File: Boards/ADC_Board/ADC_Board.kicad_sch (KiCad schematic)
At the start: 52 parts, among them J1 DE9_Pins, J10 Conn_01x04, J11 Conn_01x03, J12 Conn_01x03, J13 Conn_01x03, J14 Conn_01x03, J15 Conn_01x03, J17 Conn_01x04, J18 Conn_01x04, J19 Conn_01x04, J2 USB_B_Micro, J20 Conn_01x04, J21 Conn_01x04, J3 Conn_02x05_Odd_Even, J4 Conn_01x05, J5 Conn_01x05, J6 Conn_01x05, J7 Conn_01x03, J8 Conn_01x03, J9 DE9_Socket, U1 STM32G0B1RCTx, U5 BD50HC5WEFJ-E2, Y2 Crystal 8MHz

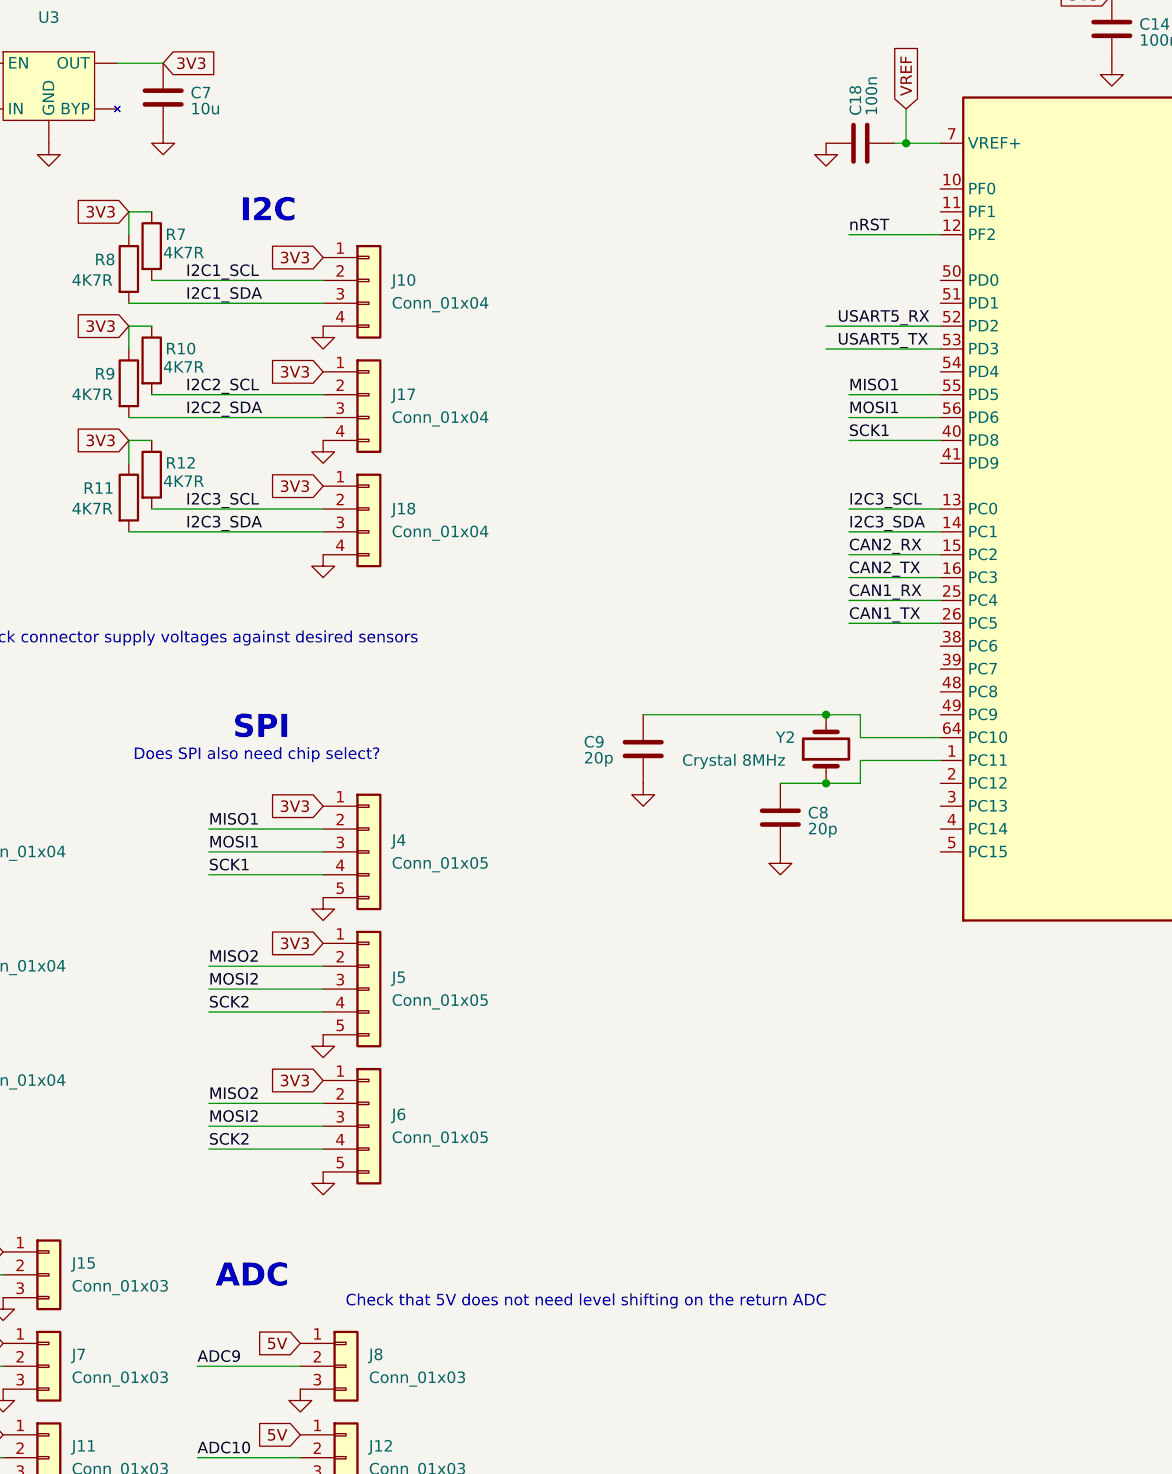
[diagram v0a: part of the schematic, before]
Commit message: Footprints for the servo and ADC board
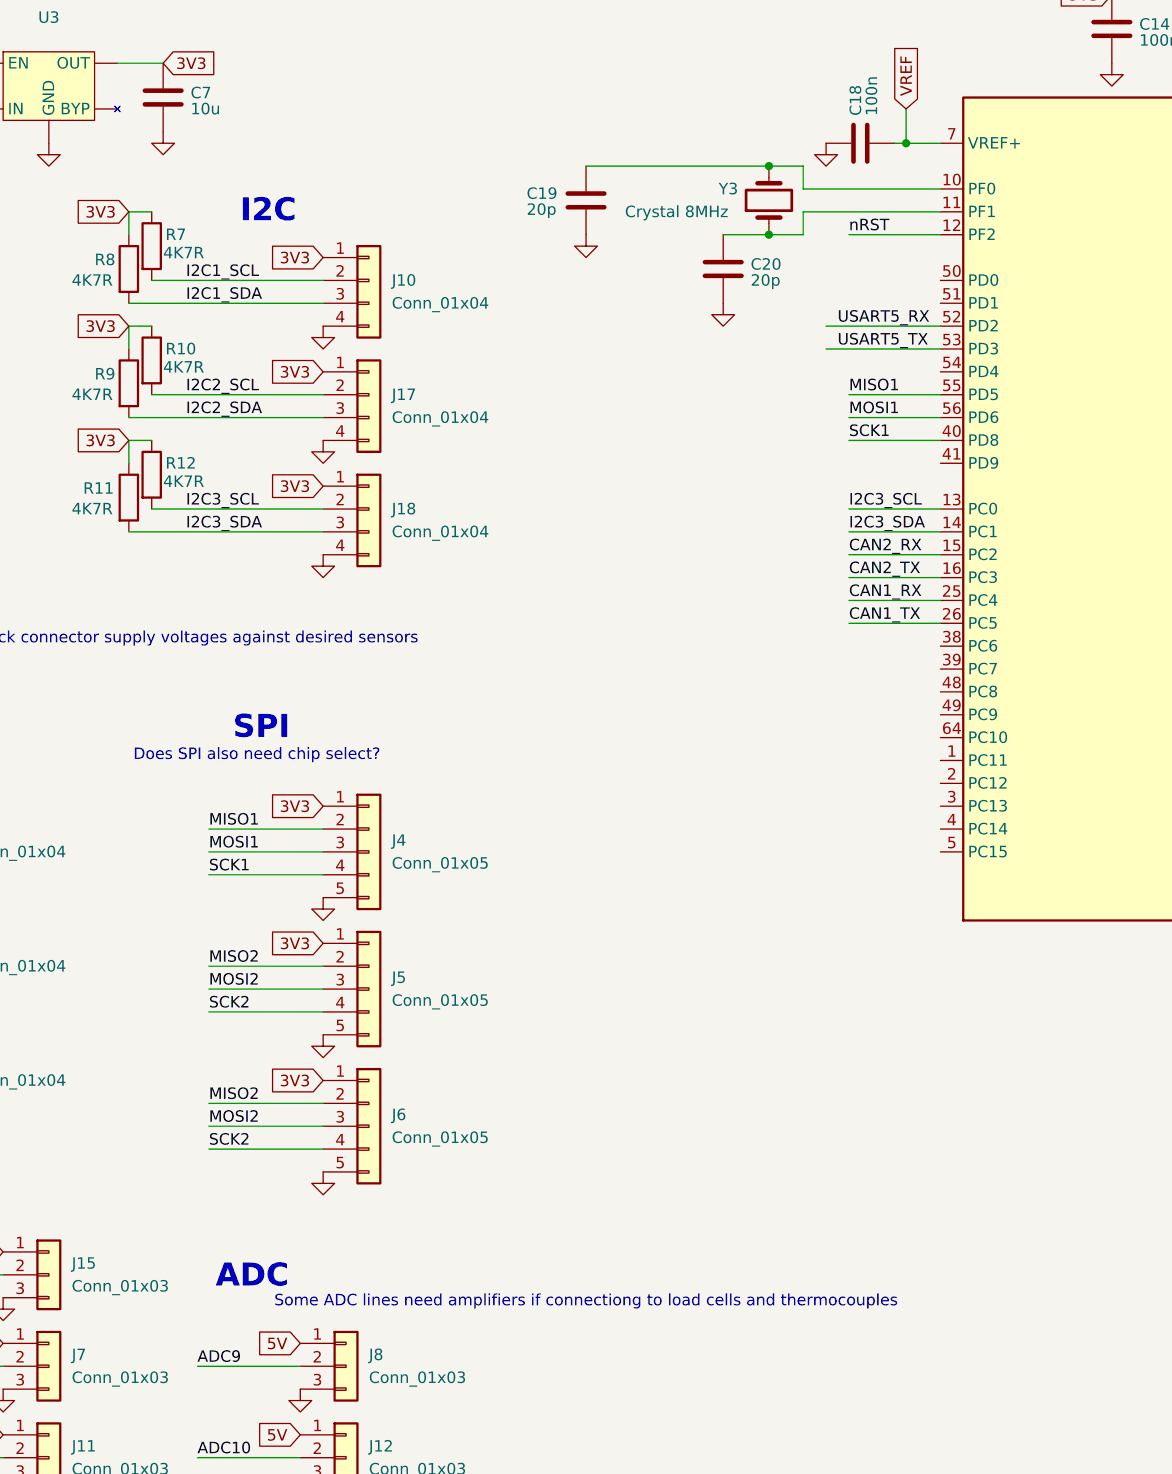
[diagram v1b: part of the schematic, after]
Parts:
- removed C8, C9: 20p, symbol Device:C
- removed Y2: Crystal 8MHz, symbol Device:Crystal
- added C19, C20: 20p, Capacitor_SMD:C_0603_1608Metric, symbol Device:C
- added Y3: Crystal 8MHz, Crystal:Crystal_SMD_Abracon_ABM3B-4Pin_5.0x3.2mm, symbol Device:Crystal
- C10, C11, C12, C13, C14, C15, C16, C17, C18, C6, C7: footprint (none) -> Capacitor_SMD:C_0603_1608Metric
- J1, J9: footprint (none) -> Connector_Molex:Molex_Micro-Fit_3.0_43650-0915_1x09_P3.00mm_Vertical; Part Number (none) -> 0436500916
- JP1, JP2: footprint (none) -> Connector_PinSocket_2.54mm:PinSocket_1x02_P2.54mm_Vertical
- R1, R10, R11, R12, R2, R3, R4, R5, R6, R7, R8, R9: footprint (none) -> Resistor_SMD:R_0603_1608Metric
- U3: footprint (none) -> footprints:TSOT23-5_ONS
- U4: footprint Custom:SOT23_DYY_TEX -> footprints:SOT23_DYY_TEX
- U5: footprint HTSOP-J8_ROM -> footprints:HTSOP-J8_ROM
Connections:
- net GND: now also C19.2, C20.2
- net at U1.10 (PF0): now also C19.1, Y3.2
- net at U1.11 (PF1): now also C20.1, Y3.1
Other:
- note added: "Some ADC lines need amplifiers if connectiong to load cells and thermocouples"
- note removed: "Check that 5V does not need level shifting on the return ADC"

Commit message: Ongoing changes to satellite  boards and test code
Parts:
- removed C16: 1u, Capacitor_SMD:C_0603_1608Metric, symbol Device:C
- removed C17: 4.7u, Capacitor_SMD:C_0603_1608Metric, symbol Device:C
- removed J1: DE9_Pins, Connector_Molex:Molex_Micro-Fit_3.0_43650-0915_1x09_P3.00mm_Vertical, symbol Connector:DE9_Pins
- removed J10, J17, J18, J19, J20, J21: Conn_01x04, symbol Connector_Generic:Conn_01x04
- removed J11, J12, J13, J14, J15, J7, J8: Conn_01x03, symbol Connector_Generic:Conn_01x03
- removed J2: USB_B_Micro, Connector_USB:USB_Micro-AB_Molex_47590-0001, symbol Connector:USB_B_Micro
- removed J3: Conn_02x05_Odd_Even, Connector_IDC:IDC-Header_2x05_P2.54mm_Vertical, symbol Connector_Generic:Conn_02x05_Odd_Even
- removed J4, J5, J6: Conn_01x05, symbol Connector_Generic:Conn_01x05
- removed J9: DE9_Socket, Connector_Molex:Molex_Micro-Fit_3.0_43650-0915_1x09_P3.00mm_Vertical, symbol Connector:DE9_Socket
- removed JP1, JP2: Jumper_2_Bridged, Connector_PinSocket_2.54mm:PinSocket_1x02_P2.54mm_Vertical, symbol Jumper:Jumper_2_Bridged
- removed R1, R2, R3, R4: 60, Resistor_SMD:R_0603_1608Metric, symbol Device:R
- removed R11: 4K7R, Resistor_SMD:R_0603_1608Metric, symbol Device:R
- removed R5: 27R, Resistor_SMD:R_0603_1608Metric, symbol Device:R
- removed U1: STM32G0B1RCTx, Package_QFP:LQFP-64_10x10mm_P0.5mm, symbol MCU_ST_STM32G0:STM32G0B1RCTx
- removed U3: ~, footprints:TSOT23-5_ONS, symbol 0_Custom_Symbols:CAT6219
- removed U4: ~, footprints:SOT23_DYY_TEX, symbol Interface_CAN_LIN:TCAN1046AV-Q1
- removed U5: BD50HC5WEFJ-E2, footprints:HTSOP-J8_ROM, symbol 0_Custom_Symbols:BD50HC5WEFJ-E2
- removed Y3: Crystal 8MHz, Crystal:Crystal_SMD_Abracon_ABM3B-4Pin_5.0x3.2mm, symbol Device:Crystal
- added C8, C9: 100n, Capacitor_SMD:C_0402_1005Metric, symbol Device:C
- added H1, H2, H3, H4: ~, MountingHole:MountingHole_3.2mm_M3_DIN965_Pad_TopOnly, symbol Mechanical:MountingHole_Pad
- added TP10: CANTX2, TestPoint:TestPoint_Pad_1.5x1.5mm, symbol Connector:TestPoint_Small
- added TP11: CANRX2, TestPoint:TestPoint_Pad_1.5x1.5mm, symbol Connector:TestPoint_Small
- added TP12: CONT2, TestPoint:TestPoint_Pad_1.5x1.5mm, symbol Connector:TestPoint_Small
- added TP13: CONT1, TestPoint:TestPoint_Pad_1.5x1.5mm, symbol Connector:TestPoint_Small
- added TP14: RS422TX, TestPoint:TestPoint_Pad_1.5x1.5mm, symbol Connector:TestPoint_Small
- added TP15: OXSNE, TestPoint:TestPoint_Pad_1.5x1.5mm, symbol Connector:TestPoint_Small
- added TP16: RS422RX, TestPoint:TestPoint_Pad_1.5x1.5mm, symbol Connector:TestPoint_Small
- added TP17: SNE12, TestPoint:TestPoint_Pad_1.5x1.5mm, symbol Connector:TestPoint_Small
- added TP18: OXFIRE, TestPoint:TestPoint_Pad_1.5x1.5mm, symbol Connector:TestPoint_Small
- added TP19: EMCH2, TestPoint:TestPoint_Pad_1.5x1.5mm, symbol Connector:TestPoint_Small
- added TP2: ADC4S, TestPoint:TestPoint_Pad_1.5x1.5mm, symbol Connector:TestPoint_Small
- added TP20: EMCH1, TestPoint:TestPoint_Pad_1.5x1.5mm, symbol Connector:TestPoint_Small
- added TP21: ARMSIG, TestPoint:TestPoint_Pad_1.5x1.5mm, symbol Connector:TestPoint_Small
- added TP3: ADC2S, TestPoint:TestPoint_Pad_1.5x1.5mm, symbol Connector:TestPoint_Small
- added TP31: ADC2, TestPoint:TestPoint_Pad_1.5x1.5mm, symbol Connector:TestPoint_Small
- added TP32: ADC3, TestPoint:TestPoint_Pad_1.5x1.5mm, symbol Connector:TestPoint_Small
- added TP4: SPISCK, TestPoint:TestPoint_Pad_1.5x1.5mm, symbol Connector:TestPoint_Small
- added TP5: SPIMISO, TestPoint:TestPoint_Pad_1.5x1.5mm, symbol Connector:TestPoint_Small
- added TP7: SPICS, TestPoint:TestPoint_Pad_1.5x1.5mm, symbol Connector:TestPoint_Small
- added TP8: CANTX1, TestPoint:TestPoint_Pad_1.5x1.5mm, symbol Connector:TestPoint_Small
- added TP9: CANRX1, TestPoint:TestPoint_Pad_1.5x1.5mm, symbol Connector:TestPoint_Small
- added U2: STM32G0B1RCTx, Package_QFP:LQFP-64_10x10mm_P0.5mm, symbol MCU_ST_STM32G0:STM32G0B1RCTx
- added U3: TCAN1046, Custom:SOT23_DYY_TEX, symbol Interface_CAN_LIN:TCAN1046AV-Q1
- added Y1: 8MHz, Crystal:Crystal_SMD_Abracon_ABM8G-4Pin_3.2x2.5mm, symbol Device:Crystal
- added Y2: 32.768k, Crystal:Crystal_SMD_2012-2Pin_2.0x1.2mm, symbol Device:Crystal
- C10: value 100n -> 4u7
- C11, C12: value 100n -> ?; footprint Capacitor_SMD:C_0603_1608Metric -> Capacitor_SMD:C_0402_1005Metric; now not fitted; now left out of the parts list
- C13: value 4u7 -> 100n
- C15: value 1u -> 100n
- C19, C20: value 20p -> 12p; footprint Capacitor_SMD:C_0603_1608Metric -> Capacitor_SMD:C_0402_1005Metric
- C6: value 10u -> 100n; footprint Capacitor_SMD:C_0603_1608Metric -> Capacitor_SMD:C_0402_1005Metric
- C7: value 10u -> 4u7
- R10, R12, R8, R9: value 4K7R -> 60.4R
- R7: value 4K7R -> 27R
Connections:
- net CAN1_RX: now also TP9.1, U2.27 (PB0), U3.1 (TXD1)
- net CAN1_TX: now also TP8.1, U2.28 (PB1), U3.4 (RXD1)
- net CAN2_RX: now also TP10.1, U2.25 (PC4), U3.6 (TXD2)
- net CAN2_TX: now also TP11.1, U2.26 (PC5), U3.7 (RXD2)
- net CANH1: now also R8.1, U3.13 (CANH1)
- net CANH2: now also R10.1, U3.9 (CANL2)
- net CANL1: now also R9.2, U3.12 (CANL1)
- net CANL2: now also R12.2, U3.10 (CANH2)
- net GND: now also C15.1, C8.2, C9.2, H1.1, H2.1, H3.1, H4.1, U2.9 (VSS), U3.2 (GND), U3.5 (GND); no longer C15.2
- net I2C1_SCL: now also U2.62 (PB8); no longer R7.2
- net I2C1_SDA: now also U2.63 (PB9); no longer R8.2
- net I2C2_SCL: now also U2.57 (PB3); no longer R10.2
- net I2C2_SDA: now also U2.58 (PB4); no longer R9.2
- net I2C3_SCL: now also U2.13 (PC0); no longer R12.2
- net I2C3_SDA: now also U2.14 (PC1)
- net SWCLK: now also U2.46 (PA14)
- net SWDIO: now also U2.45 (PA13)
- net USART1_RX: now also TP16.1, U2.61 (PB7)
- net USART1_TX: now also TP14.1, U2.60 (PB6)
- net at C20.1: now also U2.5 (PC15), Y2.1
- net at C19.1: now also U2.4 (PC14), Y2.2
- net at R6.1: now also U2.43 (PA9/PA11)
- removed net 3V3: C10.1, C12.1, C13.1, C14.1, C7.1, R10.1, R12.1, R7.1, R8.1, R9.1
- removed net 5V: C11.1, C15.1, C6.1
- net D_P renamed USB_D-
- net VREF: no longer names the net of C18.2
- net VREF: now also R10.2, R12.1
- new net: C11.1, U2.10 (PF0), Y1.1
- new net: C12.1, U2.11 (PF1), Y1.3 (2)
- new net: R7.1, U2.44 (PA10/PA12)
- new net: C15.2, R8.2, R9.1
- new net +3V3: C10.1, C14.1, C6.1, C7.1, C8.1, C9.1, U2.6 (VBAT), U2.7 (VREF+), U2.8 (VDD), U3.11 (VIO)
- new net +5V: C13.1, U3.3 (VCC)
- new net 12V_SENSE: TP17.1, U2.49 (PC9)
- new net ADC_0 (4S): TP2.1, U2.17 (PA0)
- new net ADC_1 (2S): TP3.1, U2.18 (PA1)
- new net ADC_2: TP31.1, U2.19 (PA2)
- new net ADC_3: TP32.1, U2.20 (PA3)
- new net ARM_HS: TP21.1, U2.3 (PC13)
- new net CAN1_AUX: U2.33 (PB13)
- new net CAN2_AUX: U2.32 (PB12)
- new net E1: U2.51 (PD1)
- new net E2: U2.52 (PD2)
- new net E3: U2.53 (PD3)
- new net E4: U2.54 (PD4)
- new net EMATCH_1_CONT: TP13.1, U2.39 (PC7)
- new net EMATCH_1_FIRE: TP20.1, U2.2 (PC12)
- new net EMATCH_2_CONT: TP12.1, U2.38 (PC6)
- new net EMATCH_2_FIRE: TP19.1, U2.1 (PC11)
- new net IMON_HS: U2.35 (PB15)
- new net LED1: U2.50 (PD0)
- new net NRST: U2.12 (PF2)
- new net OX_FIRE: TP18.1, U2.64 (PC10)
- new net OX_LOW_SENSE: TP15.1, U2.48 (PC8)
- new net PGOOD_HS: U2.34 (PB14)
- new net SPI_MISO: TP5.1, U2.23 (PA6)
- new net SPI_SCK: TP4.1, U2.22 (PA5)
- new net SPI_SD_CS: TP7.1, U2.21 (PA4)
- new net UART2_RX: U2.56 (PD6)
- new net UART2_TX: U2.55 (PD5)
- new net USB_D+: R7.2
- no-connect marks 0 -> 14
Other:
- added sheet Analog Domain (Analog.kicad_sch)
- note added: "CAN"
- note added: "MCU"
- note removed: "ADC"
- note removed: "Check connector supply voltages against desired sensors"
- note removed: "Does SPI also need chip select?"
- note removed: "I2C"
- note removed: "SPI"
- note removed: "Some ADC lines need amplifiers if connectiong to load cells and thermocouples"
- note removed: "USART"

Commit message: Somewhat done servo+adc boards
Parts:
- removed C15, C18: 100n, Capacitor_SMD:C_0603_1608Metric, symbol Device:C
- removed C19, C20: 12p, Capacitor_SMD:C_0402_1005Metric, symbol Device:C
- removed TP10: CANTX2, TestPoint:TestPoint_Pad_1.5x1.5mm, symbol Connector:TestPoint_Small
- removed TP11: CANRX2, TestPoint:TestPoint_Pad_1.5x1.5mm, symbol Connector:TestPoint_Small
- removed TP12: CONT2, TestPoint:TestPoint_Pad_1.5x1.5mm, symbol Connector:TestPoint_Small
- removed TP13: CONT1, TestPoint:TestPoint_Pad_1.5x1.5mm, symbol Connector:TestPoint_Small
- removed TP14: RS422TX, TestPoint:TestPoint_Pad_1.5x1.5mm, symbol Connector:TestPoint_Small
- removed TP15: OXSNE, TestPoint:TestPoint_Pad_1.5x1.5mm, symbol Connector:TestPoint_Small
- removed TP16: RS422RX, TestPoint:TestPoint_Pad_1.5x1.5mm, symbol Connector:TestPoint_Small
- removed TP17: SNE12, TestPoint:TestPoint_Pad_1.5x1.5mm, symbol Connector:TestPoint_Small
- removed TP18: OXFIRE, TestPoint:TestPoint_Pad_1.5x1.5mm, symbol Connector:TestPoint_Small
- removed TP19: EMCH2, TestPoint:TestPoint_Pad_1.5x1.5mm, symbol Connector:TestPoint_Small
- removed TP2: ADC4S, TestPoint:TestPoint_Pad_1.5x1.5mm, symbol Connector:TestPoint_Small
- removed TP20: EMCH1, TestPoint:TestPoint_Pad_1.5x1.5mm, symbol Connector:TestPoint_Small
- removed TP21: ARMSIG, TestPoint:TestPoint_Pad_1.5x1.5mm, symbol Connector:TestPoint_Small
- removed TP3: ADC2S, TestPoint:TestPoint_Pad_1.5x1.5mm, symbol Connector:TestPoint_Small
- removed TP31: ADC2, TestPoint:TestPoint_Pad_1.5x1.5mm, symbol Connector:TestPoint_Small
- removed TP32: ADC3, TestPoint:TestPoint_Pad_1.5x1.5mm, symbol Connector:TestPoint_Small
- removed TP4: SPISCK, TestPoint:TestPoint_Pad_1.5x1.5mm, symbol Connector:TestPoint_Small
- removed TP5: SPIMISO, TestPoint:TestPoint_Pad_1.5x1.5mm, symbol Connector:TestPoint_Small
- removed TP7: SPICS, TestPoint:TestPoint_Pad_1.5x1.5mm, symbol Connector:TestPoint_Small
- removed Y2: 32.768k, Crystal:Crystal_SMD_2012-2Pin_2.0x1.2mm, symbol Device:Crystal
- added C10, C12: 22u, Capacitor_SMD:C_1206_3216Metric, symbol Device:C
- added C11, C13: 10u, Capacitor_SMD:C_0603_1608Metric, symbol Device:C
- added C14: 100u, Capacitor_SMD:CP_Elec_8x10.5, symbol Device:C_Polarized
- added D1, D2: PESD3V3L4UW, Package_TO_SOT_SMD:SOT-665, symbol Power_Protection:PESD3V3L4UW
- added D3: 18V, Diode_SMD:D_SOD-323F, symbol Device:D_Zener
- added D4: 9V 15.4VC, Diode_SMD:D_SOD-123F, symbol Device:D_TVS
- added D5: LED_R, LED_SMD:LED_1206_3216Metric, symbol Device:LED
- added D6: LED_G, LED_SMD:LED_1206_3216Metric, symbol Device:LED
- added D7: LED_B, LED_SMD:LED_1206_3216Metric, symbol Device:LED
- added F1, F2: 2A, symbol Device:Fuse
- added J1: SWD JST PH, Connector_JST:JST_PH_B4B-PH-K_1x04_P2.00mm_Vertical, symbol Connector_Generic:Conn_01x04
- added J10: I2CC JST, Connector_JST:JST_PH_B5B-PH-K_1x05_P2.00mm_Vertical, symbol Connector_Generic:Conn_01x05
- added J11, J6: DB9 Microfit, Connector_Molex:Molex_Micro-Fit_3.0_43045-1012_2x05_P3.00mm_Vertical, symbol Connector:DE9_Socket
- added J12: AUX BATT CONN, Connector_JST:JST_PH_B4B-PH-K_1x04_P2.00mm_Vertical, symbol Connector_Generic:Conn_01x04
- added J2: UART JST, Connector_JST:JST_PH_B3B-PH-K_1x03_P2.00mm_Vertical, symbol Connector_Generic:Conn_01x03
- added J3: Extras JST, Connector_JST:JST_PH_B7B-PH-K_1x07_P2.00mm_Vertical, symbol Connector_Generic:Conn_01x07
- added J4: USB_B_Micro, Connector_USB:USB_Micro-B_Amphenol_10118193-0001LF_Horizontal, symbol Connector:USB_B_Micro
- added J5: I2CA JST, Connector_JST:JST_PH_B5B-PH-K_1x05_P2.00mm_Vertical, symbol Connector_Generic:Conn_01x05
- added J7: I2CB JST, Connector_JST:JST_PH_B5B-PH-K_1x05_P2.00mm_Vertical, symbol Connector_Generic:Conn_01x05
- added J8, J9: CAN1_T, Connector_PinHeader_2.54mm:PinHeader_1x02_P2.54mm_Vertical, symbol Connector_Generic:Conn_01x02
- added JP1: CH SEL, symbol Jumper:SolderJumper_3_Bridged12
- added JP2: CL SEL, symbol Jumper:SolderJumper_3_Bridged12
- added Q1: DMP6023LFG, Package_SON:Diodes_PowerDI3333-8, symbol Transistor_FET:DMP3013SFV
- added R1, R2, R3: 0R, Resistor_SMD:R_0603_1608Metric, symbol Device:R
- added R11, R7: 100K, symbol Device:R
- added R13, R14: 220R, Resistor_SMD:R_0603_1608Metric, symbol Device:R
- added R15: 14K3, Resistor_SMD:R_0603_1608Metric, symbol Device:R
- added R16: 100K, Resistor_SMD:R_0603_1608Metric, symbol Device:R
- added R17: 9K53, Resistor_SMD:R_0603_1608Metric, symbol Device:R
- added R6: 120R, symbol Device:R
- added U3: AZ1117C-3.3, Package_TO_SOT_SMD:SOT-223-3_TabPin2, symbol Regulator_Linear:AZ1117-3.3
- added U4: AZ1117C-5.0, Package_TO_SOT_SMD:SOT-223-3_TabPin2, symbol Regulator_Linear:AZ1117-5.0
- R10, R9: value 60.4R -> 100K; footprint Resistor_SMD:R_0603_1608Metric -> (none)
- R12: value 60.4R -> 549R
- R8: value 60.4R -> 120R; footprint Resistor_SMD:R_0603_1608Metric -> (none)
- renumbered C8 to C1, C6 to C2, C7 to C3, C10 to C4, C9 to C5, C11 to C6, C12 to C7, C14 to C8, C13 to C9, R6 to R4, R7 to R5, TP9 to TP1, TP8 to TP2, U2 to U1, U3 to U2
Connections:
- net OX_FIRE is gone; now on net CAN1_AUX: U1.64 (PC10)
- net USART1_RX is gone; now on net CAN2_AUX: U1.61 (PB7)
- net +3V3: now also R10.1, R9.1, C10.1, J10.5 (Pin_5), J5.5 (Pin_5), J7.5 (Pin_5), R1.1, R11.2, R7.2, U3.2 (VO)
- net +5V: now also C11.1, C12.1, J10.3 (Pin_3), J5.3 (Pin_3), J7.3 (Pin_3), R2.1, U3.3 (VI), U4.2 (VO)
- net CAN1_AUX: now also J6.3; no longer U1.33 (PB13)
- net CAN1_RX: now also U1.62 (PB8); no longer U1.27 (PB0)
- net CAN1_TX: now also U1.63 (PB9); no longer U1.28 (PB1)
- net CAN2_AUX: now also J11.3; no longer U1.32 (PB12)
- net CANH1: now also J11.6, J6.6, J8.1 (Pin_1), JP1.1 (A); no longer R8.1, U2.13 (CANH1)
- net CANH2: now also J11.8, J6.8, JP1.3 (B), R6.2; no longer R10.1, U2.9 (CANL2)
- net CANL1: now also J11.7, J6.7, J9.1 (Pin_1), JP2.1 (A); no longer R9.2, U2.12 (CANL1)
- net CANL2: now also R8.2, J11.9, J6.9, JP2.3 (B); no longer R12.2, U2.10 (CANH2)
- net E1: now also J3.2 (Pin_2)
- net E2: now also J3.3 (Pin_3)
- net E3: now also J3.5 (Pin_5)
- net E4: now also J3.6 (Pin_6)
- net GND: now also C10.2, C11.2, C12.2, C13.2, C14.2, D1.2 (A), D2.2 (A), D4.1 (A1), D5.1 (K), D6.1 (K), D7.1 (K), J1.2 (Pin_2), J10.1 (Pin_1), J11.2, J11.4, J12.3 (Pin_3), J12.4 (Pin_4), J2.2 (Pin_2), J3.1 (Pin_1), J3.7 (Pin_7), J4.5 (GND), J5.1 (Pin_1), J6.2, J6.4, J7.1 (Pin_1), R16.2, R17.2, U3.1 (GND), U4.1 (GND)
- net I2C1_SCL: now also U1.37 (PA9/UCPD1_DBCC1), D2.3 (K2), J5.4 (Pin_4); no longer U1.62 (PB8)
- net I2C1_SDA: now also U1.42 (PA10/UCPD1_DBCC2), D2.1 (K1), J5.2 (Pin_2); no longer U1.63 (PB9)
- net I2C2_SCL: now also D2.5 (K4), J7.4 (Pin_4)
- net I2C2_SDA: now also D2.4 (K3), J7.2 (Pin_2)
- net I2C3_SCL: now also D1.3 (K2), J10.4 (Pin_4)
- net I2C3_SDA: now also D1.1 (K1), J10.2 (Pin_2)
- net LED1: now also R13.1
- net NRST: now also J1.4 (Pin_4)
- net SPI_MOSI: now also U1.24 (PA7)
- net SWCLK: now also J1.1 (Pin_1)
- net SWDIO: now also J1.3 (Pin_3)
- net UART2_RX: now also D1.4 (K3), J2.1 (Pin_1)
- net UART2_TX: now also D1.5 (K4), J2.3 (Pin_3)
- net USB_D+: now also J4.3 (D+)
- net USB_D-: now also J4.2 (D-)
- net at R10.2: now also U2.7 (RXD2); no longer R12.1
- net at U2.14 (STB1): now also R7.1
- net at U2.8 (STB2): now also R11.1
- net 2S+ A10: now reaches U1.29 (PB2)
- net 2S+ A10: now also R15.2, R17.1
- net A11: now reaches U1.30 (PB10)
- net 12V_SENSE renamed LED2
- net LED2: now also R14.1
- net ADC_0 (4S) renamed CJT A0
- net ADC_1 (2S) renamed MIPA_A A1
- net ADC_2 renamed MIPA_B A2
- net ADC_3 renamed MIPA_C A3
- net ARM_HS: no longer names the net of U1.3 (PC13)
- net CAN2_RX: no longer names the net of U2.6 (TXD2)
- net CAN2_RX: now also R9.2; no longer U1.25 (PC4)
- net CAN2_TX renamed ~{ADC_RDY}
- net ~{ADC_RDY}: no longer U2.7 (RXD2)
- net EMATCH_1_CONT: no longer names the net of U1.39 (PC7)
- net EMATCH_1_FIRE: no longer names the net of U1.2 (PC12)
- net EMATCH_2_CONT: no longer names the net of U1.38 (PC6)
- net EMATCH_2_FIRE: no longer names the net of U1.1 (PC11)
- net IMON_HS: no longer names the net of U1.35 (PB15)
- net OX_LOW_SENSE: no longer names the net of U1.48 (PC8)
- net PGOOD_HS: no longer names the net of U1.34 (PB14)
- net USART1_TX: no longer names the net of U1.60 (PB6)
- new net: D7.2 (A), R14.2
- new net: D3.2 (A), Q1.4 (G), R16.1
- new net: D4.2 (A2), F1.1, F2.2, Q1.5 (D)
- new net: J3.4 (Pin_4), R1.2, R2.2, R3.2
- new net: D6.2 (A), R13.2
- new net: F2.1, J12.1 (Pin_1), J12.2 (Pin_2)
- new net: J9.2 (Pin_2), R8.1
- new net: D5.2 (A), R12.2
- new net: J8.2 (Pin_2), R6.1
- new net +7V4: C13.1, C14.1, D3.1 (K), Q1.1 (S), Q1.2 (S), Q1.3 (S), R12.1, R15.1, R3.1, U4.3 (VI)
- new net +7V4_CAN: F1.2, J11.1, J11.5, J6.1, J6.5
- new net A9: U1.28 (PB1)
- new net CANH: JP1.2 (C), U2.13 (CANH1)
- new net CANL: JP2.2 (C), U2.12 (CANL1)
- new net SYNC: U1.25 (PC4)
- new net ~{ADC_RST}: U1.27 (PB0)
- no-connect marks 14 -> 12
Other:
- sheet Analog Domain ports: added DIN, DOUT, MIPA_A, MIPA_B, MIPA_C, SCLK, START_SYNC, THERMISOR, ~{CS}, ~{DRDY}, ~{RESET}; removed none
- note added: "ANALOG"
- note added: "Extras"
- note added: "I^{2}C"
- note added: "POWER INPUT"
- note added: "SWD"
- note added: "UART"
- note added: "USB"
- moved on the sheet: C1, C2, C3, C4, C5, C6, C7, C8, C9, H1, H2, H3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

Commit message: Fixes and footprints
Just thermocouples todo
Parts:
- added TP10: SCK, TestPoint:TestPoint_Pad_1.5x1.5mm, symbol Connector:TestPoint_Small
- added TP11: MISO, TestPoint:TestPoint_Pad_1.5x1.5mm, symbol Connector:TestPoint_Small
- added TP12: MOSI, TestPoint:TestPoint_Pad_1.5x1.5mm, symbol Connector:TestPoint_Small
- added TP13: SYNC, TestPoint:TestPoint_Pad_1.5x1.5mm, symbol Connector:TestPoint_Small
- added TP14: ADC_RDY, TestPoint:TestPoint_Pad_1.5x1.5mm, symbol Connector:TestPoint_Small
- added TP15: ADC_RST, TestPoint:TestPoint_Pad_1.5x1.5mm, symbol Connector:TestPoint_Small
- added TP24: 7.4V, TestPoint:TestPoint_Pad_1.5x1.5mm, symbol Connector:TestPoint
- added TP25: 5V, TestPoint:TestPoint_Pad_1.5x1.5mm, symbol Connector:TestPoint
- added TP26: 3.3V, TestPoint:TestPoint_Pad_1.5x1.5mm, symbol Connector:TestPoint
- added TP27, TP28: GND, TestPoint:TestPoint_Bridge_Pitch2.54mm_Drill1.3mm, symbol Connector:TestPoint
- added TP3: A9, TestPoint:TestPoint_Pad_1.5x1.5mm, symbol Connector:TestPoint_Small
- added TP4: A11, TestPoint:TestPoint_Pad_1.5x1.5mm, symbol Connector:TestPoint_Small
- added TP5: CJT, TestPoint:TestPoint_Pad_1.5x1.5mm, symbol Connector:TestPoint_Small
- added TP6: MIP1, TestPoint:TestPoint_Pad_1.5x1.5mm, symbol Connector:TestPoint_Small
- added TP7: MIP2, TestPoint:TestPoint_Pad_1.5x1.5mm, symbol Connector:TestPoint_Small
- added TP8: MIP3, TestPoint:TestPoint_Pad_1.5x1.5mm, symbol Connector:TestPoint_Small
- added TP9: CS, TestPoint:TestPoint_Pad_1.5x1.5mm, symbol Connector:TestPoint_Small
- F1, F2: footprint (none) -> Fuse:Fuse_1206_3216Metric
- JP1, JP2: footprint (none) -> Jumper:SolderJumper-3_P1.3mm_Bridged12_RoundedPad1.0x1.5mm
- R10, R11, R6, R7, R8, R9: footprint (none) -> Resistor_SMD:R_0603_1608Metric
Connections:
- net +3V3: now also TP26.1
- net +5V: now also TP25.1
- net +7V4: now also TP24.1
- net A11: now also TP4.1
- net A9: now also TP3.1
- net CJT A0: now also TP5.1
- net GND: now also TP27.1, TP28.1
- net MIPA_A A1: now also TP6.1
- net MIPA_B A2: now also TP7.1
- net MIPA_C A3: now also TP8.1
- net SPI_MISO: now also TP11.1
- net SPI_MOSI: now also TP12.1
- net SPI_SCK: now also TP10.1
- net SPI_SD_CS: now also TP9.1
- net SYNC: now also TP13.1
- net ~{ADC_RDY}: now also TP14.1
- net ~{ADC_RST}: now also TP15.1
- no-connect marks 12 -> 26
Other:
- moved on the sheet: D5, D6, D7, H1, H2, H3, H4, R12, R13, R14
